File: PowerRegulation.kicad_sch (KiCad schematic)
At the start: 52 parts, among them J10 XT60-M, J11 24V_Lockout_Key_Switch, J21 Logic_Power_Switch, K1 G5Q-1A DC24, Q11 BSS138, Q7 BSS138, Q9 ZXMP3A17E6TA, U10 LM3880-1AA, U11 LM66200DRLR, U6 TPS5430DDA, U7 TPS78533QKVURQ1, U9 TPS78450QDBVRQ1

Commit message: add 2 stage lockout to ignitor, add ignitor resistance reading with adc current source
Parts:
- renumbered C14 to C1, C38 to C10, C41 to C11, C16 to C2, C15 to C3, C18 to C4, C20 to C5, C17 to C6, C39 to C7, C40 to C8, C19 to C9, D8 to D1, D9 to D2, D10 to D3, D11 to D4, D14 to D5, D15 to D6, D16 to D7, J21 to J1, J10 to J2, J11 to J3, Q7 to Q1, Q11 to Q2, Q9 to Q3, R32 to R10, R33 to R11, R67 to R12, R68 to R13, R69 to R14, R34 to R15, R35 to R16, R72 to R17, R73 to R18, R74 to R19, R70 to R20, R71 to R21, R38 to R22, R39 to R23, R37 to R24, R30 to R25, R40 to R26, R29 to R8, R31 to R9, U10 to U1, U6 to U2, U7 to U3, U9 to U4, U11 to U5
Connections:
- net +24V: now also K1.5; no longer K1.1
- net +24V_POST_LCKT: now also K1.3; no longer K1.2
- net +24V_SAFE: now also K1.2; no longer K1.3
- net at D4.2 (A), Q1.3 (D): now also K1.1; no longer K1.5
- net LCKT_RLY_CTRL_FET: no longer names the net of Q1.1 (G), R15.1, R16.1
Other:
- moved on the sheet: K1

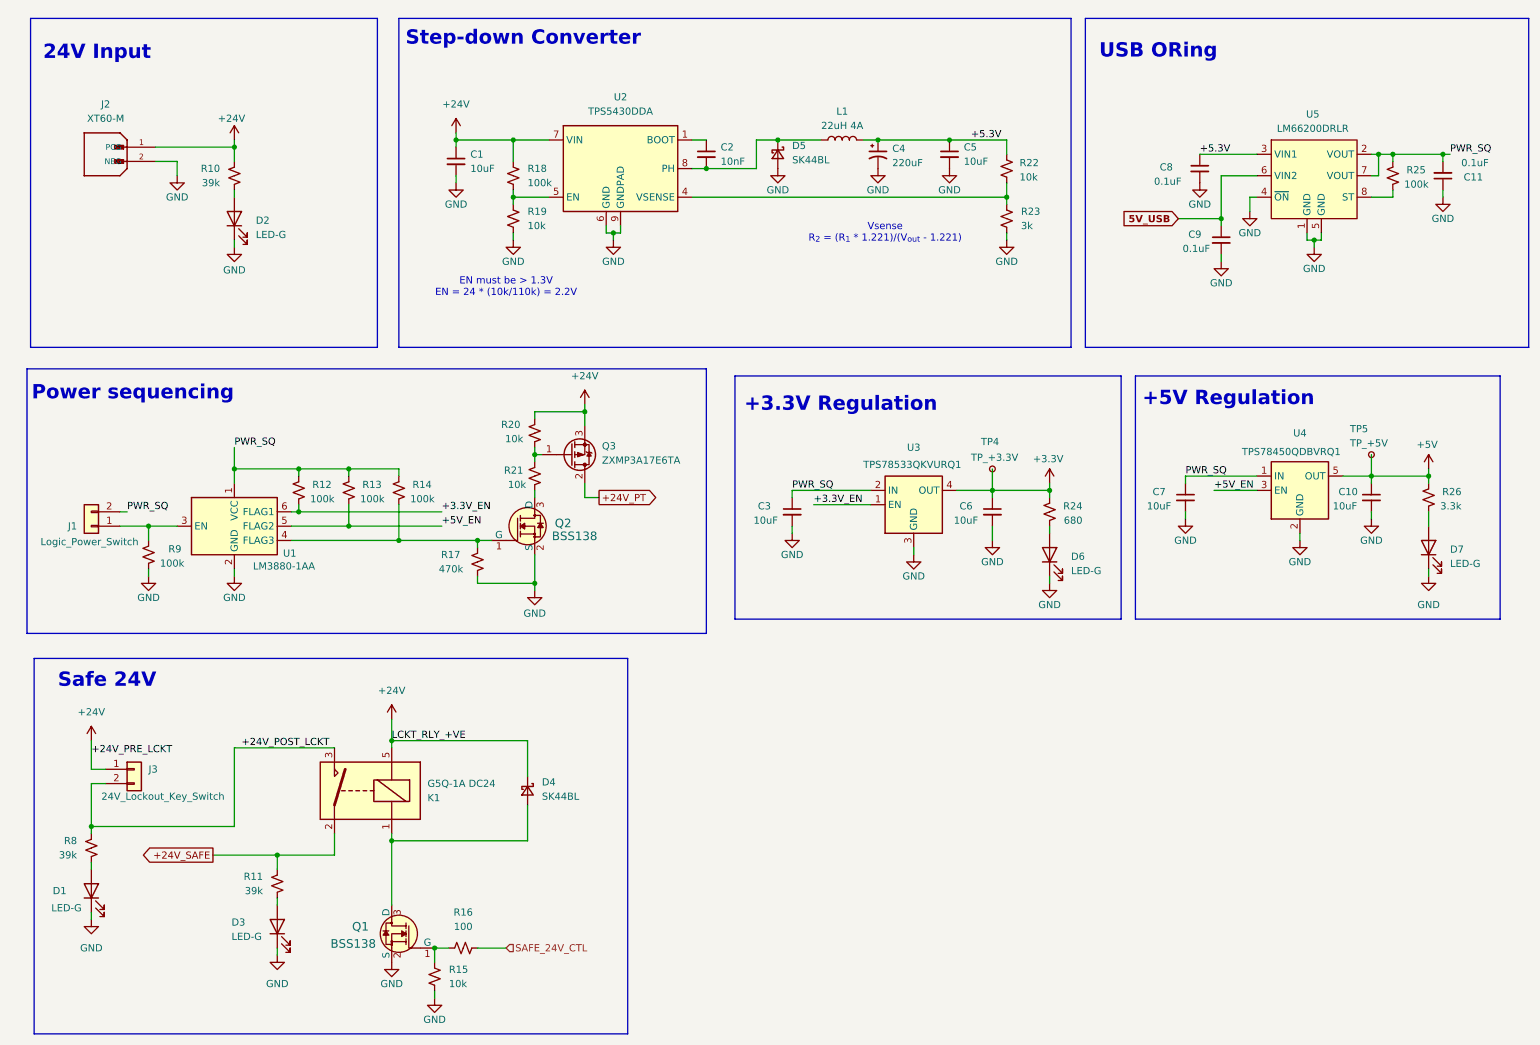
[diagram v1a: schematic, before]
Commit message: add periodic buzzer alert to +24V_SAFE
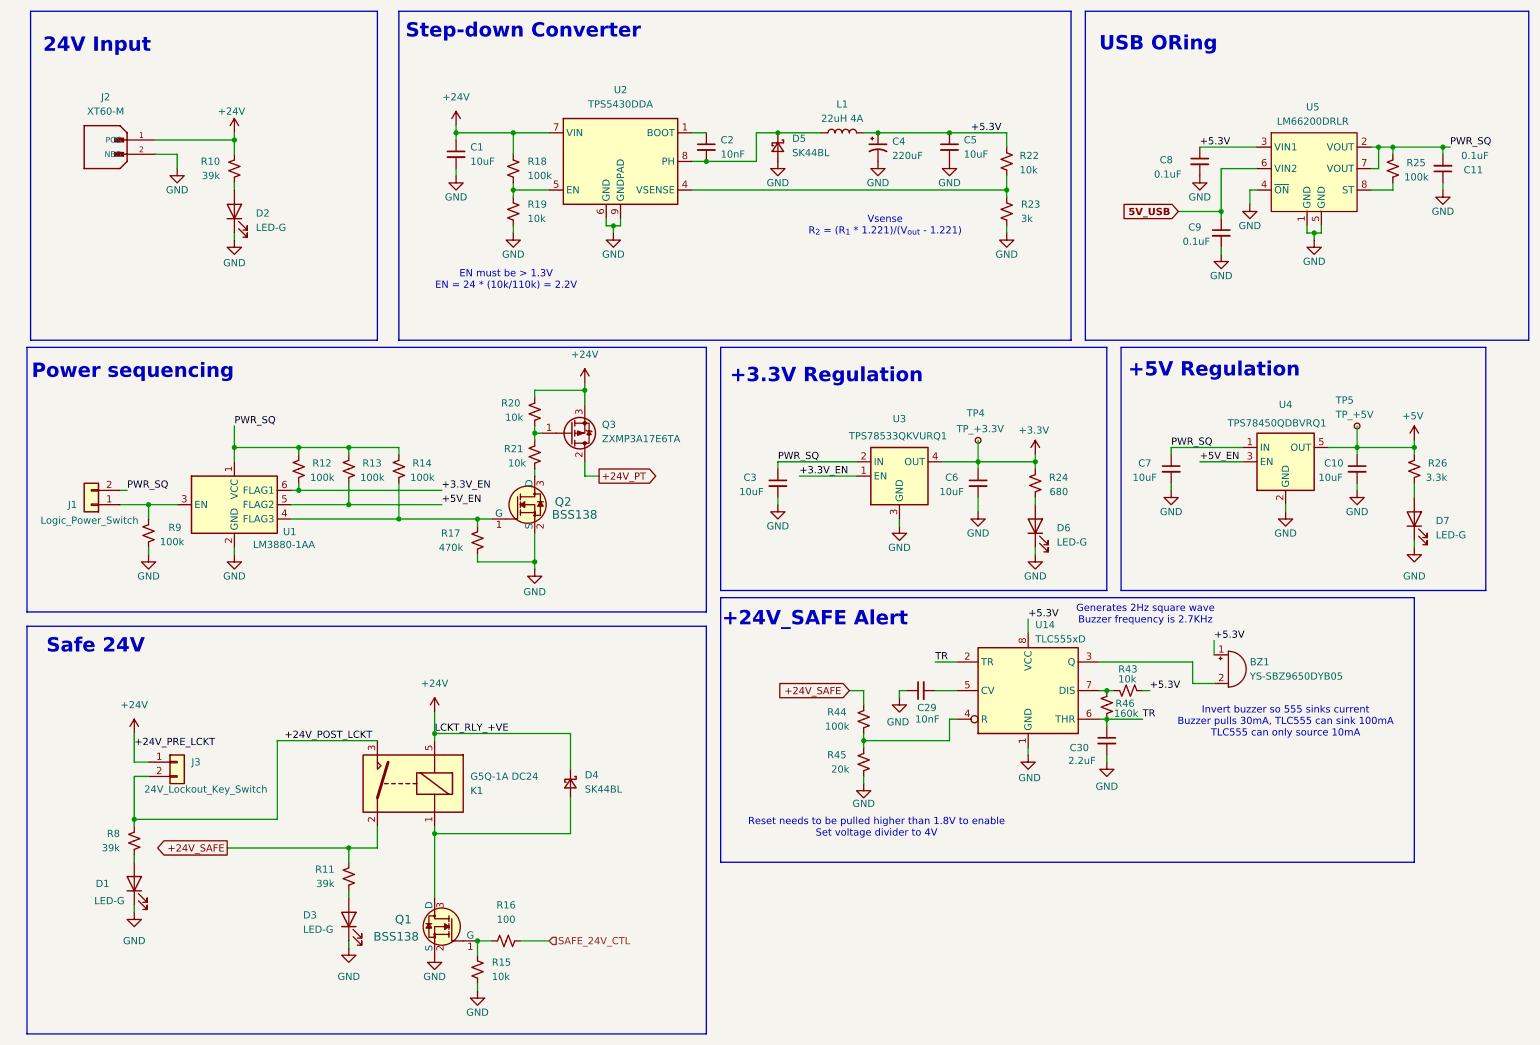
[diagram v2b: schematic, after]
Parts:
- added BZ1: YS-SBZ9650DYB05, symbol Device:Buzzer
- added C29: 10nF, Capacitor_SMD:C_1206_3216Metric, symbol Device:C_Small
- added C30: 2.2uF, Capacitor_SMD:C_1206_3216Metric, symbol Device:C_Small
- added R43: 10k, Resistor_SMD:R_0402_1005Metric, symbol Device:R_Small_US
- added R44: 100k, Resistor_SMD:R_0402_1005Metric, symbol Device:R_Small_US
- added R45: 20k, Resistor_SMD:R_0402_1005Metric, symbol Device:R_Small_US
- added R46: 160k, Resistor_SMD:R_0402_1005Metric, symbol Device:R_Small_US
- added U14: TLC555xD, Package_SO:SOIC-8_3.9x4.9mm_P1.27mm, symbol Timer:TLC555xD
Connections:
- net +24V_SAFE: now also R44.2
- net +5.3V: now also BZ1.1 (+), R43.2, U14.8 (VCC)
- net GND: now also C29.1, C30.2, R45.1, U14.1 (GND)
- new net: BZ1.2 (-), U14.3 (Q)
- new net: R44.1, R45.2, U14.4 (R)
- new net: C29.2, U14.5 (CV)
- new net: R43.1, R46.1, U14.7 (DIS)
- new net TR: C30.1, R46.2, U14.2 (TR), U14.6 (THR)
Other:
- note added: "+24V_SAFE Alert"
- note added: "Generates 2Hz square wave Buzzer frequency is 2.7KHz"
- note added: "Invert buzzer so 555 sinks current Buzzer pulls 30mA, TLC555 can sink 100mA TLC555 can only source 10mA"
- note added: "Reset needs to be pulled higher than 1.8V to enable Set voltage divider to 4V"
- moved on the sheet: C1, C10, C11, C2, C3, C4, C5, C6, C7, C8, C9, D1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

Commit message: ground floating trace between ign relays when relays open
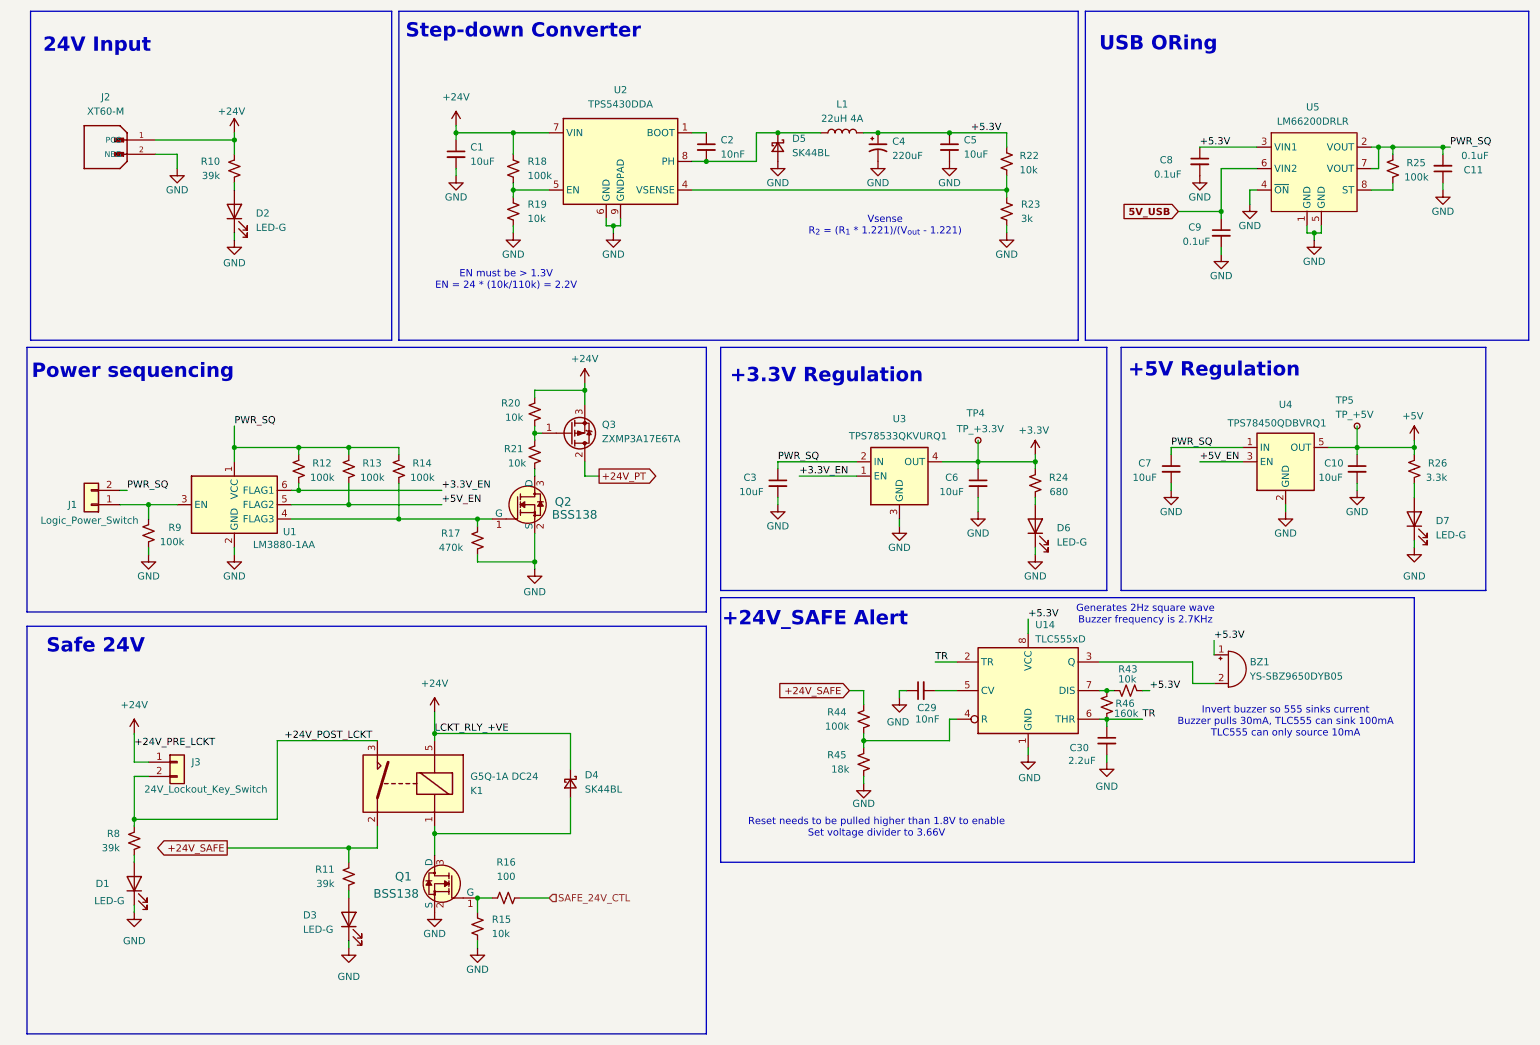
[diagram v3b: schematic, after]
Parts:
- R45: value 20k -> 18k
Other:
- note added: "Reset needs to be pulled higher than 1.8V to enable Set voltage divider to 3.66V"
- note removed: "Reset needs to be pulled higher than 1.8V to enable Set voltage divider to 4V"
- moved on the sheet: Q1, R15, R16
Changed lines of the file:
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@@
 	(rectangle
 		(start 80.01 13.97)
-		(end 199.39 72.39)
+		(end 200.66 72.39)
 		(stroke
 			(width 0)
@@
 	(rectangle
 		(start 14.605 13.97)
-		(end 76.2 72.39)
+		(end 78.74 72.39)
 		(stroke
 			(width 0)
@@
 		)
 	)
-	(text "Reset needs to be pulled higher than 1.8V to enable\nSet voltage divider to 4V"
+	(text "Reset needs to be pulled higher than 1.8V to enable\nSet voltage divider to 3.66V"
 		(exclude_from_sim no)
 		(at 164.846 159.004 0)
@@
 	)
 	(junction
-		(at 93.98 179.07)
+		(at 93.98 171.45)
 		(diameter 0)
 		(color 0 0 0 0)
@@
 	(wire
 		(pts
-			(xy 93.98 187.96) (xy 93.98 186.69)
+			(xy 93.98 180.34) (xy 93.98 179.07)
 		)
 		(stroke
@@
 	(wire
 		(pts
-			(xy 93.98 179.07) (xy 93.98 181.61)
+			(xy 93.98 171.45) (xy 93.98 173.99)
 		)
 		(stroke
@@
 	(wire
 		(pts
+			(xy 86.36 160.02) (xy 86.36 163.83)
+		)
+		(stroke
+			(width 0)
+			(type default)
+		)
+	)
+	(wire
+		(pts
 			(xy 50.8 36.83) (xy 50.8 39.37)
 		)
@@
 	(wire
 		(pts
-			(xy 93.98 179.07) (xy 96.52 179.07)
+			(xy 93.98 171.45) (xy 96.52 171.45)
 		)
 		(stroke
@@
 	(wire
 		(pts
-			(xy 86.36 160.02) (xy 86.36 171.45)
-		)
-		(stroke
-			(width 0)
-			(type default)
-		)
-	)
-	(wire
-		(pts
 			(xy 237.49 101.6) (xy 237.49 102.87)
 		)
@@
 	(wire
 		(pts
-			(xy 86.36 160.02) (xy 86.36 158.75)
-		)
-		(stroke
-			(width 0)
-			(type default)
-		)
-	)
-	(wire
-		(pts
 			(xy 71.12 101.6) (xy 71.12 97.79)
 		)
@@
 	(wire
 		(pts
+			(xy 86.36 158.75) (xy 86.36 160.02)
+		)
+		(stroke
+			(width 0)
+			(type default)
+		)
+	)
+	(wire
+		(pts
 			(xy 60.96 101.6) (xy 71.12 101.6)
 		)
@@
 	(wire
 		(pts
-			(xy 101.6 179.07) (xy 106.68 179.07)
+			(xy 101.6 171.45) (xy 106.68 171.45)
 		)
 		(stroke
@@
 	(hierarchical_label "SAFE_24V_CTL"
 		(shape input)
-		(at 106.68 179.07 0)
+		(at 106.68 171.45 0)
 		(effects
 			(font
@@
 	(symbol
 		(lib_id "Device:R_Small_US")
-		(at 99.06 179.07 90)
+		(at 99.06 171.45 90)
 		(unit 1)
 		(exclude_from_sim no)
@@
 		(fields_autoplaced yes)
 		(property "Reference" "R16"
-			(at 99.06 172.72 90)
+			(at 99.06 165.1 90)
 			(effects
 				(font
@@
 		)
 		(property "Value" "100"
-			(at 99.06 175.26 90)
+			(at 99.06 167.64 90)
 			(effects
 				(font
@@
 		)
 		(property "Footprint" "Resistor_SMD:R_0402_1005Metric"
-			(at 99.06 179.07 0)
+			(at 99.06 171.45 0)
 			(effects
 				(font
@@
 		)
 		(property "Datasheet" "~"
-			(at 99.06 179.07 0)
+			(at 99.06 171.45 0)
 			(effects
 				(font
@@
 		)
 		(property "Description" "Resistor, small US symbol"
-			(at 99.06 179.07 0)
+			(at 99.06 171.45 0)
 			(effects
 				(font
@@
 		)
 		(property "MPN" "0402WGF1000TCE"
-			(at 99.06 179.07 90)
+			(at 99.06 171.45 90)
 			(effects
 				(font
@@
 		)
 		(property "LCSC" "C25076"
-			(at 99.06 179.07 90)
+			(at 99.06 171.45 90)
 			(effects
 				(font
@@
 	(symbol
 		(lib_id "Device:R_Small_US")
-		(at 93.98 184.15 0)
+		(at 93.98 176.53 0)
 		(unit 1)
 		(exclude_from_sim no)
@@
 		(fields_autoplaced yes)
 		(property "Reference" "R15"
-			(at 96.52 182.8799 0)
+			(at 96.52 175.2599 0)
 			(effects
 				(font
@@
 		)
 		(property "Value" "10k"
-			(at 96.52 185.4199 0)
+			(at 96.52 177.7999 0)
 			(effects
 				(font
@@
 		)
 		(property "Footprint" "Resistor_SMD:R_0402_1005Metric"
-			(at 93.98 184.15 0)
+			(at 93.98 176.53 0)
 			(effects
 				(font
@@
 		)
 		(property "Datasheet" "~"
-			(at 93.98 184.15 0)
+			(at 93.98 176.53 0)
 			(effects
 				(font
@@
 		)
 		(property "Description" "Resistor, small US symbol"
-			(at 93.98 184.15 0)
+			(at 93.98 176.53 0)
 			(effects
 				(font
@@
 		)
 		(property "LCSC" "C25531"
-			(at 93.98 184.15 0)
+			(at 93.98 176.53 0)
 			(effects
 				(font
@@
 		)
 		(property "MPN" "0402WGJ0103TCE"
-			(at 93.98 184.15 0)
+			(at 93.98 176.53 0)
 			(effects
 				(font
@@
 	(symbol
 		(lib_id "power:GND")
-		(at 93.98 187.96 0)
+		(at 93.98 180.34 0)
 		(unit 1)
 		(exclude_from_sim no)
@@
 		(dnp no)
 		(property "Reference" "#PWR031"
-			(at 93.98 194.31 0)
+			(at 93.98 186.69 0)
 			(effects
 				(font
@@
 		)
 		(property "Value" "GND"
-			(at 93.98 191.77 0)
+			(at 93.98 184.15 0)
 			(effects
 				(font
@@
 		)
 		(property "Footprint" ""
-			(at 93.98 187.96 0)
+			(at 93.98 180.34 0)
 			(effects
 				(font
@@
 		)
 		(property "Datasheet" ""
-			(at 93.98 187.96 0)
+			(at 93.98 180.34 0)
 			(effects
 				(font
@@
 		)
 		(property "Description" "Power symbol creates a global label with name \"GND\" , ground"
-			(at 93.98 187.96 0)
+			(at 93.98 180.34 0)
 			(effects
 				(font
@@
 	(symbol
 		(lib_id "dk_Transistors-FETs-MOSFETs-Single:BSS138")
-		(at 86.36 176.53 0)
+		(at 86.36 168.91 0)
 		(mirror y)
 		(unit 1)
@@
 		(dnp no)
 		(property "Reference" "Q1"
-			(at 82.296 175.2601 0)
+			(at 82.296 167.6401 0)
 			(effects
 				(font
@@
 		)
 		(property "Value" "BSS138"
-			(at 83.566 178.308 0)
+			(at 83.566 170.688 0)
 			(effects
 				(font
@@
 		)
 		(property "Footprint" "Package_TO_SOT_SMD:SOT-23-3"
-			(at 81.28 171.45 0)
+			(at 81.28 163.83 0)
 			(effects
 				(font
@@
 		)
 		(property "Datasheet" "https://www.onsemi.com/pub/Collateral/BSS138-D.PDF"
-			(at 81.28 168.91 0)
+			(at 81.28 161.29 0)
 			(effects
 				(font
@@
 		)
 		(property "Description" "MOSFET N-CH 50V 220MA SOT-23"
-			(at 86.36 176.53 0)
+			(at 86.36 168.91 0)
 			(effects
 				(font
@@
 		)
 		(property "MPN" "BSS138"
-			(at 81.28 163.83 0)
+			(at 81.28 156.21 0)
 			(effects
 				(font
@@
 		)
 		(property "LCSC" "C8490"
-			(at 86.36 176.53 0)
+			(at 86.36 168.91 0)
 			(effects
 				(font
@@
 		)
 		(property "Category" "Discrete Semiconductor Products"
-			(at 81.28 161.29 0)
+			(at 81.28 153.67 0)
 			(effects
 				(font
@@
 		)
 		(property "Family" "Transistors - FETs, MOSFETs - Single"
-			(at 81.28 158.75 0)
+			(at 81.28 151.13 0)
 			(effects
 				(font
@@
 		)
 		(property "DK_Datasheet_Link" "https://www.onsemi.com/pub/Collateral/BSS138-D.PDF"
-			(at 81.28 156.21 0)
+			(at 81.28 148.59 0)
 			(effects
 				(font
@@
 		)
 		(property "DK_Detail_Page" "/product-detail/en/on-semiconductor/BSS138/BSS138CT-ND/244294"
-			(at 81.28 153.67 0)
+			(at 81.28 146.05 0)
 			(effects
 				(font
@@
 		)
 		(property "Description_1" "MOSFET N-CH 50V 220MA SOT-23"
-			(at 81.28 151.13 0)
+			(at 81.28 143.51 0)
 			(effects
 				(font
@@
 		)
 		(property "Manufacturer" "ON Semiconductor"
-			(at 81.28 148.59 0)
+			(at 81.28 140.97 0)
 			(effects
 				(font
@@
 		)
 		(property "Status" "Active"
-			(at 81.28 146.05 0)
+			(at 81.28 138.43 0)
 			(effects
 				(font
@@
 		(on_board yes)
 		(dnp no)
-		(fields_autoplaced yes)
 		(property "Reference" "#PWR036"
 			(at 113.03 83.82 0)
@@
 		)
 		(property "Value" "+24V"
-			(at 113.03 74.93 0)
+			(at 113.03 75.692 0)
 			(effects
 				(font
@@
 			)
 		)
-		(property "Value" "20k"
+		(property "Value" "18k"
 			(at 160.02 148.59 0)
 			(effects
@@
 	(symbol
 		(lib_id "power:GND")
-		(at 86.36 181.61 0)
+		(at 86.36 173.99 0)
 		(unit 1)
 		(exclude_from_sim no)
@@
 		(dnp no)
 		(property "Reference" "#PWR030"
-			(at 86.36 187.96 0)
+			(at 86.36 180.34 0)
 			(effects
 				(font
@@
 		)
 		(property "Value" "GND"
-			(at 86.36 185.42 0)
+			(at 86.36 177.8 0)
 			(effects
 				(font
@@
 		)
 		(property "Footprint" ""
-			(at 86.36 181.61 0)
+			(at 86.36 173.99 0)
 			(effects
 				(font
@@
 		)
 		(property "Datasheet" ""
-			(at 86.36 181.61 0)
+			(at 86.36 173.99 0)
 			(effects
 				(font
@@
 		)
 		(property "Description" "Power symbol creates a global label with name \"GND\" , ground"
-			(at 86.36 181.61 0)
+			(at 86.36 173.99 0)
 			(effects
 				(font
